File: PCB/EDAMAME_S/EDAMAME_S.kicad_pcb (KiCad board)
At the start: 2 copper layers, 80 x 87 mm, 60 parts, among them CN1 USB-B-MICRO, J1 Conn_01x20, J2 Conn_01x20, J5 Nichrome, J6 CHARGE, M1 Motor_L, M2 Motor_R, Q1 NDS9936, Q2 FDS4675, Q3 2SC2712, SW1 power, U1 microSD, U2 FT231XS, U3 ESP32-WROOM, U4 NJM2391DL1-33, U5 LSM303C, U6 GPS-54D, U7 BD6231F, U8 INA226, U9 BD6231F

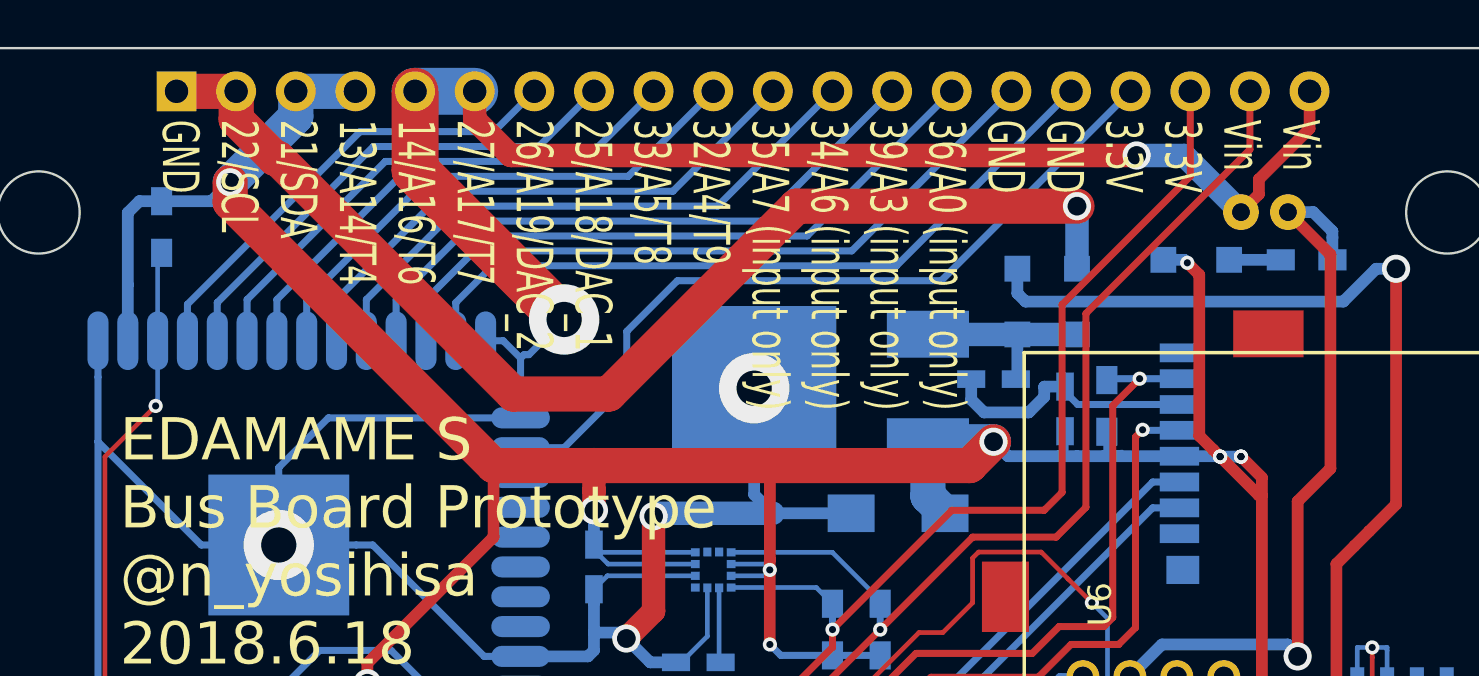
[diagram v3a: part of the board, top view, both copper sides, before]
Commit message: ピンアサインシルクの修正
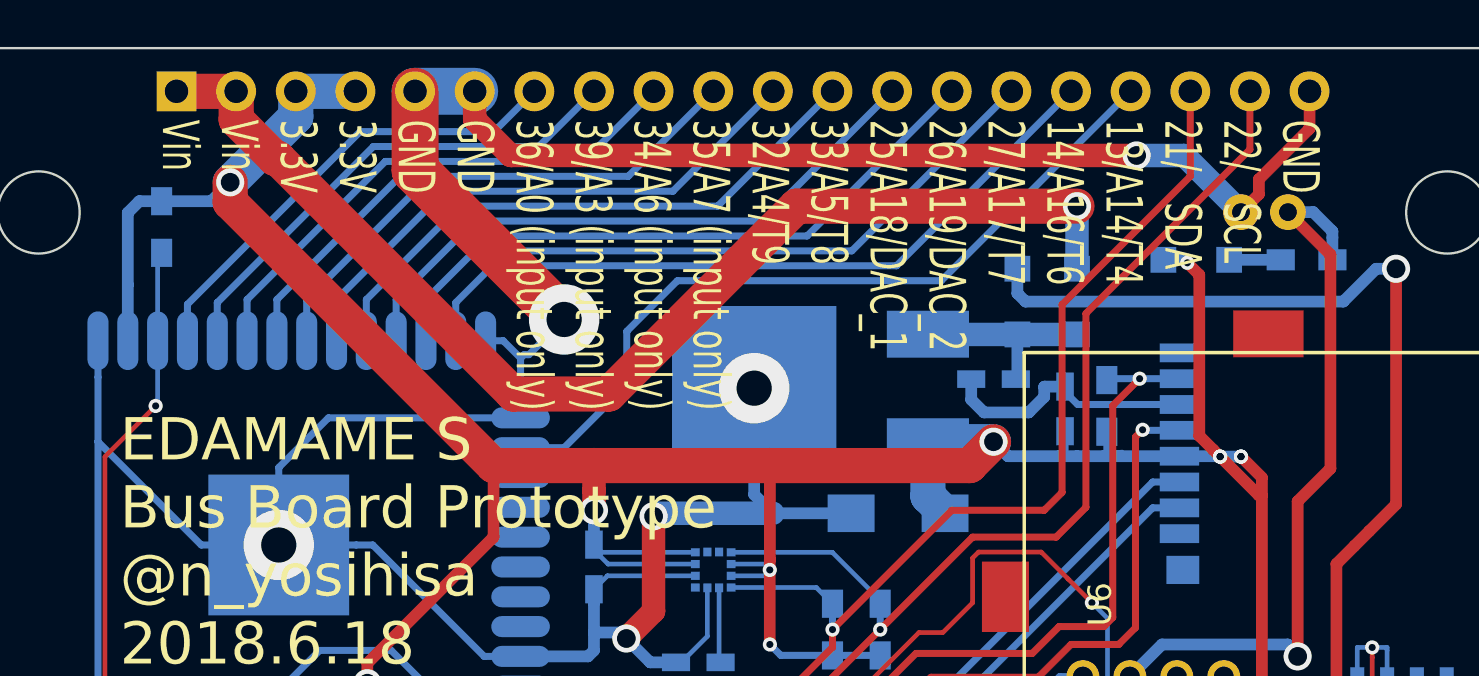
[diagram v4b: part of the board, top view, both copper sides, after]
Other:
- board text added: "GND 22/ SCL 21/ SDA 13/A14/T4 14/A16/T6 27/A17/T7 26/A19/DAC_2 25/A18/DAC_1 33/A5/T8 32/A4/T9 35/A7 (input only) 34/A6 (input only) 39/A3 (input only) 36/A0 (input only) GND GND 3.3V 3.3V Vin Vin"
- board text removed: "Vin Vin 3.3V 3.3V GND GND 36/A0 (input only) 39/A3 (input only) 34/A6 (input only) 35/A7 (input only) 32/A4/T9 33/A5/T8 25/A18/DAC_1 26/A19/DAC_2 27/A17/T7 14/A16/T6 13/A14/T4 21/SDA 22/SCL GND"
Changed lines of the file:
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@@
-(kicad_pcb (version 4) (host pcbnew 4.0.7)
+(kicad_pcb (version 20171130) (host pcbnew "(5.0.0)")
   (general
-    (links 175)
-    (no_connects 0)
-    (area 25.338472 14.29792 128.401872 110.608941)
     (thickness 1.6)
     (drawings 60)
@@
       (layerselection 0x010f0_80000001)
       (usegerberextensions true)
+      (usegerberattributes false)
+      (usegerberadvancedattributes false)
+      (creategerberjobfile false)
       (excludeedgelayer true)
       (linewidth 0.100000)
@@
       (hpglpennumber 1)
       (hpglpenspeed 20)
-      (hpglpendiameter 15)
-      (hpglpenoverlay 2)
+      (hpglpendiameter 15.000000)
       (psnegative false)
       (psa4output false)
@@
       (drillshape 0)
       (scaleselection 1)
-      (outputdirectory edamame_s/))
+      (outputdirectory "edamame_s/"))
   )
   (net 0 "")
@@
     (at 74.525872 97.67694 180)
     (fp_text reference G*** (at 0 0 180) (layer B.SilkS) hide
-      (effects (font (thickness 0.3)) (justify mirror))
+      (effects (font (size 1.524 1.524) (thickness 0.3)) (justify mirror))
     )
     (fp_text value LOGO (at 0.254 0 180) (layer B.SilkS) hide
-      (effects (font (thickness 0.3)) (justify mirror))
+      (effects (font (size 1.524 1.524) (thickness 0.3)) (justify mirror))
     )
     (fp_poly (pts (xy 15.24 -5.4356) (xy -15.24 -5.4356) (xy -15.24 -2.772206) (xy -14.3256 -2.772206)
@@
       (effects (font (size 1 1) (thickness 0.15)) (justify mirror))
     )
-    (fp_text user "Espressif Systems" (at -6.858 0.889 360) (layer B.SilkS)
+    (fp_text user "Espressif Systems" (at -6.858 0.889) (layer B.SilkS)
       (effects (font (size 1 1) (thickness 0.15)) (justify mirror))
     )
     (fp_circle (center 9.906 -6.604) (end 10.033 -6.858) (layer B.SilkS) (width 0.5))
-    (fp_text user ESP32-WROOM (at 6 1.25 360) (layer B.SilkS)
+    (fp_text user ESP32-WROOM (at 6 1.25) (layer B.SilkS)
       (effects (font (size 1 1) (thickness 0.15)) (justify mirror))
     )
@@
       (effects (font (size 1 1) (thickness 0.15)))
     )
-    (fp_text value 10440 (at -1.27 0 360) (layer F.Fab)
+    (fp_text value 10440 (at -1.27 0) (layer F.Fab)
       (effects (font (size 1 1) (thickness 0.15)))
     )
@@
       (net 2 GND))
     (model ${KISYS3DMOD}/Socket_Strips.3dshapes/Socket_Strip_Straight_1x20_Pitch2.54mm.wrl
-      (at (xyz 0 -0.95 0))
+      (offset (xyz 0 -24.12999963760376 0))
       (scale (xyz 1 1 1))
       (rotate (xyz 0 0 270))
@@
   (module EH:B2B-EH (layer F.Cu)
     (at 95.281272 72.81954 270)
-    (fp_text reference M2 (at -4.6066 -0.0726 360) (layer F.SilkS)
+    (fp_text reference M2 (at -4.6066 -0.0726) (layer F.SilkS)
       (effects (font (size 1 1) (thickness 0.15)))
     )
-    (fp_text value Motor_R (at 4.7914 -0.0726 360) (layer F.SilkS)
+    (fp_text value Motor_R (at 4.7914 -0.0726) (layer F.SilkS)
       (effects (font (size 1 1) (thickness 0.15)))
     )
@@
     (tags SOT-23)
     (attr smd)
-    (fp_text reference Q3 (at 3.556 0 360) (layer B.SilkS)
+    (fp_text reference Q3 (at 3.556 0) (layer B.SilkS)
       (effects (font (size 1 1) (thickness 0.15)) (justify mirror))
     )
@@
       (effects (font (size 1 1) (thickness 0.15)) (justify mirror))
     )
-    (fp_text user %R (at 0 0 540) (layer B.Fab)
+    (fp_text user %R (at 0 0 180) (layer B.Fab)
       (effects (font (size 0.5 0.5) (thickness 0.075)) (justify mirror))
     )
@@
     (descr "MicroSD Card socket, Molex P/N 502774-0811")
     (fp_text reference U1 (at 0 -4.64 270) (layer B.SilkS) hide
-      (effects (font (thickness 0.3048)) (justify mirror))
+      (effects (font (size 1.524 1.524) (thickness 0.3048)) (justify mirror))
     )
     (fp_text value microSD (at 0 0.44 270) (layer B.SilkS) hide
-      (effects (font (thickness 0.3048)) (justify mirror))
+      (effects (font (size 1.524 1.524) (thickness 0.3048)) (justify mirror))
     )
     (fp_line (start -2.90068 -7.29996) (end -4.39928 -7.59968) (layer B.SilkS) (width 0.2))
@@
   (module user:BH-411 (layer F.Cu)
     (at 68.551872 69.15894 270)
-    (fp_text reference BT3 (at 1.27 0 360) (layer F.SilkS)
+    (fp_text reference BT3 (at 1.27 0) (layer F.SilkS)
       (effects (font (size 1 1) (thickness 0.15)))
     )
-    (fp_text value 10440 (at -1.27 0 540) (layer F.Fab)
+    (fp_text value 10440 (at -1.27 0 180) (layer F.Fab)
       (effects (font (size 1 1) (thickness 0.15)))
     )
@@
     (at 57.253872 50.43294)
     (fp_text reference G*** (at 0 0) (layer F.SilkS) hide
-      (effects (font (thickness 0.3)))
+      (effects (font (size 1.524 1.524) (thickness 0.3)))
     )
     (fp_text value LOGO (at 0.75 0) (layer F.SilkS) hide
-      (effects (font (thickness 0.3)))
+      (effects (font (size 1.524 1.524) (thickness 0.3)))
     )
     (fp_poly (pts (xy 15.24 5.4356) (xy -15.24 5.4356) (xy -15.24 2.772206) (xy -14.3256 2.772206)
@@
     (effects (font (size 1.8 1.8) (thickness 0.3)) (justify left))
   )
-  (gr_text "Vin\nVin\n3.3V\n3.3V\nGND\nGND\n36/A0 (input only)\n39/A3 (input only)\n34/A6 (input only)\n35/A7 (input only)\n32/A4/T9\n33/A5/T8\n25/A18/DAC_1\n26/A19/DAC_2\n27/A17/T7\n14/A16/T6\n13/A14/T4\n21/SDA\n22/SCL\nGND\n" (at 68.429872 20.20694 270) (layer F.SilkS)
+  (gr_text "GND\n22/   SCL\n21/   SDA\n13/A14/T4\n14/A16/T6\n27/A17/T7\n26/A19/DAC_2\n25/A18/DAC_1\n33/A5/T8\n32/A4/T9\n35/A7 (input only)\n34/A6 (input only)\n39/A3 (input only)\n36/A0 (input only)\nGND\nGND\n3.3V\n3.3V\nVin\nVin" (at 68.429872 20.20694 270) (layer F.SilkS)
     (effects (font (size 1.56 1) (thickness 0.2)) (justify left))
   )

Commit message: Revert "ピンアサインシルクの修正"
This reverts commit a283f1fcbc2505a9a6d1f3c0ea775a1104c0ca35.
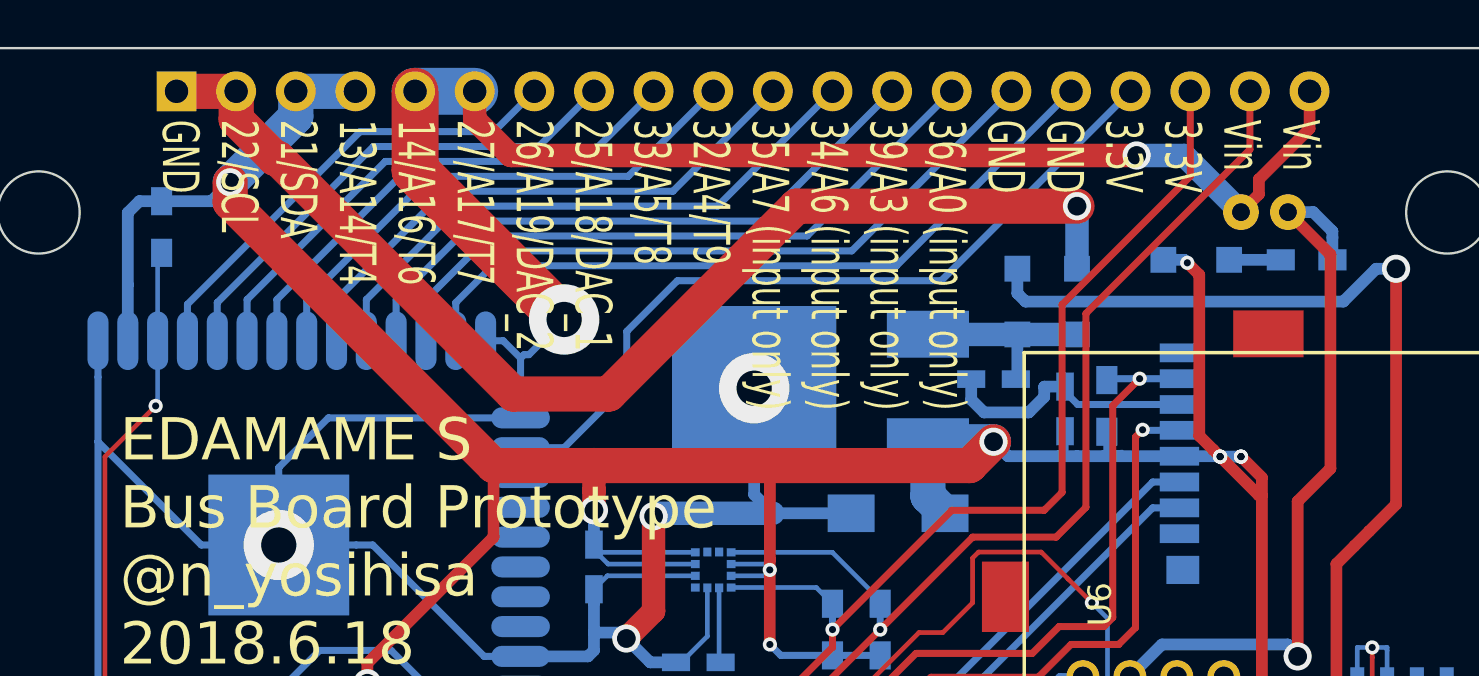
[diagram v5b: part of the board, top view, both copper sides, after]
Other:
- board text added: "Vin Vin 3.3V 3.3V GND GND 36/A0 (input only) 39/A3 (input only) 34/A6 (input only) 35/A7 (input only) 32/A4/T9 33/A5/T8 25/A18/DAC_1 26/A19/DAC_2 27/A17/T7 14/A16/T6 13/A14/T4 21/SDA 22/SCL GND"
- board text removed: "GND 22/ SCL 21/ SDA 13/A14/T4 14/A16/T6 27/A17/T7 26/A19/DAC_2 25/A18/DAC_1 33/A5/T8 32/A4/T9 35/A7 (input only) 34/A6 (input only) 39/A3 (input only) 36/A0 (input only) GND GND 3.3V 3.3V Vin Vin"
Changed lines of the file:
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@@
-(kicad_pcb (version 20171130) (host pcbnew "(5.0.0)")
+(kicad_pcb (version 4) (host pcbnew 4.0.7)
   (general
+    (links 175)
+    (no_connects 0)
+    (area 25.338472 14.29792 128.401872 110.608941)
     (thickness 1.6)
     (drawings 60)
@@
       (layerselection 0x010f0_80000001)
       (usegerberextensions true)
-      (usegerberattributes false)
-      (usegerberadvancedattributes false)
-      (creategerberjobfile false)
       (excludeedgelayer true)
       (linewidth 0.100000)
@@
       (hpglpennumber 1)
       (hpglpenspeed 20)
-      (hpglpendiameter 15.000000)
+      (hpglpendiameter 15)
+      (hpglpenoverlay 2)
       (psnegative false)
       (psa4output false)
@@
       (drillshape 0)
       (scaleselection 1)
-      (outputdirectory "edamame_s/"))
+      (outputdirectory edamame_s/))
   )
   (net 0 "")
@@
     (at 74.525872 97.67694 180)
     (fp_text reference G*** (at 0 0 180) (layer B.SilkS) hide
-      (effects (font (size 1.524 1.524) (thickness 0.3)) (justify mirror))
+      (effects (font (thickness 0.3)) (justify mirror))
     )
     (fp_text value LOGO (at 0.254 0 180) (layer B.SilkS) hide
-      (effects (font (size 1.524 1.524) (thickness 0.3)) (justify mirror))
+      (effects (font (thickness 0.3)) (justify mirror))
     )
     (fp_poly (pts (xy 15.24 -5.4356) (xy -15.24 -5.4356) (xy -15.24 -2.772206) (xy -14.3256 -2.772206)
@@
       (effects (font (size 1 1) (thickness 0.15)) (justify mirror))
     )
-    (fp_text user "Espressif Systems" (at -6.858 0.889) (layer B.SilkS)
+    (fp_text user "Espressif Systems" (at -6.858 0.889 360) (layer B.SilkS)
       (effects (font (size 1 1) (thickness 0.15)) (justify mirror))
     )
     (fp_circle (center 9.906 -6.604) (end 10.033 -6.858) (layer B.SilkS) (width 0.5))
-    (fp_text user ESP32-WROOM (at 6 1.25) (layer B.SilkS)
+    (fp_text user ESP32-WROOM (at 6 1.25 360) (layer B.SilkS)
       (effects (font (size 1 1) (thickness 0.15)) (justify mirror))
     )
@@
       (effects (font (size 1 1) (thickness 0.15)))
     )
-    (fp_text value 10440 (at -1.27 0) (layer F.Fab)
+    (fp_text value 10440 (at -1.27 0 360) (layer F.Fab)
       (effects (font (size 1 1) (thickness 0.15)))
     )
@@
       (net 2 GND))
     (model ${KISYS3DMOD}/Socket_Strips.3dshapes/Socket_Strip_Straight_1x20_Pitch2.54mm.wrl
-      (offset (xyz 0 -24.12999963760376 0))
+      (at (xyz 0 -0.95 0))
       (scale (xyz 1 1 1))
       (rotate (xyz 0 0 270))
@@
   (module EH:B2B-EH (layer F.Cu)
     (at 95.281272 72.81954 270)
-    (fp_text reference M2 (at -4.6066 -0.0726) (layer F.SilkS)
+    (fp_text reference M2 (at -4.6066 -0.0726 360) (layer F.SilkS)
       (effects (font (size 1 1) (thickness 0.15)))
     )
-    (fp_text value Motor_R (at 4.7914 -0.0726) (layer F.SilkS)
+    (fp_text value Motor_R (at 4.7914 -0.0726 360) (layer F.SilkS)
       (effects (font (size 1 1) (thickness 0.15)))
     )
@@
     (tags SOT-23)
     (attr smd)
-    (fp_text reference Q3 (at 3.556 0) (layer B.SilkS)
+    (fp_text reference Q3 (at 3.556 0 360) (layer B.SilkS)
       (effects (font (size 1 1) (thickness 0.15)) (justify mirror))
     )
@@
       (effects (font (size 1 1) (thickness 0.15)) (justify mirror))
     )
-    (fp_text user %R (at 0 0 180) (layer B.Fab)
+    (fp_text user %R (at 0 0 540) (layer B.Fab)
       (effects (font (size 0.5 0.5) (thickness 0.075)) (justify mirror))
     )
@@
     (descr "MicroSD Card socket, Molex P/N 502774-0811")
     (fp_text reference U1 (at 0 -4.64 270) (layer B.SilkS) hide
-      (effects (font (size 1.524 1.524) (thickness 0.3048)) (justify mirror))
+      (effects (font (thickness 0.3048)) (justify mirror))
     )
     (fp_text value microSD (at 0 0.44 270) (layer B.SilkS) hide
-      (effects (font (size 1.524 1.524) (thickness 0.3048)) (justify mirror))
+      (effects (font (thickness 0.3048)) (justify mirror))
     )
     (fp_line (start -2.90068 -7.29996) (end -4.39928 -7.59968) (layer B.SilkS) (width 0.2))
@@
   (module user:BH-411 (layer F.Cu)
     (at 68.551872 69.15894 270)
-    (fp_text reference BT3 (at 1.27 0) (layer F.SilkS)
+    (fp_text reference BT3 (at 1.27 0 360) (layer F.SilkS)
       (effects (font (size 1 1) (thickness 0.15)))
     )
-    (fp_text value 10440 (at -1.27 0 180) (layer F.Fab)
+    (fp_text value 10440 (at -1.27 0 540) (layer F.Fab)
       (effects (font (size 1 1) (thickness 0.15)))
     )
@@
     (at 57.253872 50.43294)
     (fp_text reference G*** (at 0 0) (layer F.SilkS) hide
-      (effects (font (size 1.524 1.524) (thickness 0.3)))
+      (effects (font (thickness 0.3)))
     )
     (fp_text value LOGO (at 0.75 0) (layer F.SilkS) hide
-      (effects (font (size 1.524 1.524) (thickness 0.3)))
+      (effects (font (thickness 0.3)))
     )
     (fp_poly (pts (xy 15.24 5.4356) (xy -15.24 5.4356) (xy -15.24 2.772206) (xy -14.3256 2.772206)
@@
     (effects (font (size 1.8 1.8) (thickness 0.3)) (justify left))
   )
-  (gr_text "GND\n22/   SCL\n21/   SDA\n13/A14/T4\n14/A16/T6\n27/A17/T7\n26/A19/DAC_2\n25/A18/DAC_1\n33/A5/T8\n32/A4/T9\n35/A7 (input only)\n34/A6 (input only)\n39/A3 (input only)\n36/A0 (input only)\nGND\nGND\n3.3V\n3.3V\nVin\nVin" (at 68.429872 20.20694 270) (layer F.SilkS)
+  (gr_text "Vin\nVin\n3.3V\n3.3V\nGND\nGND\n36/A0 (input only)\n39/A3 (input only)\n34/A6 (input only)\n35/A7 (input only)\n32/A4/T9\n33/A5/T8\n25/A18/DAC_1\n26/A19/DAC_2\n27/A17/T7\n14/A16/T6\n13/A14/T4\n21/SDA\n22/SCL\nGND\n" (at 68.429872 20.20694 270) (layer F.SilkS)
     (effects (font (size 1.56 1) (thickness 0.2)) (justify left))
   )
